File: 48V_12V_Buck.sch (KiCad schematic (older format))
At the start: 63 parts, among them Q4 CSD18534Q5A, Q5 CSD18540Q5B

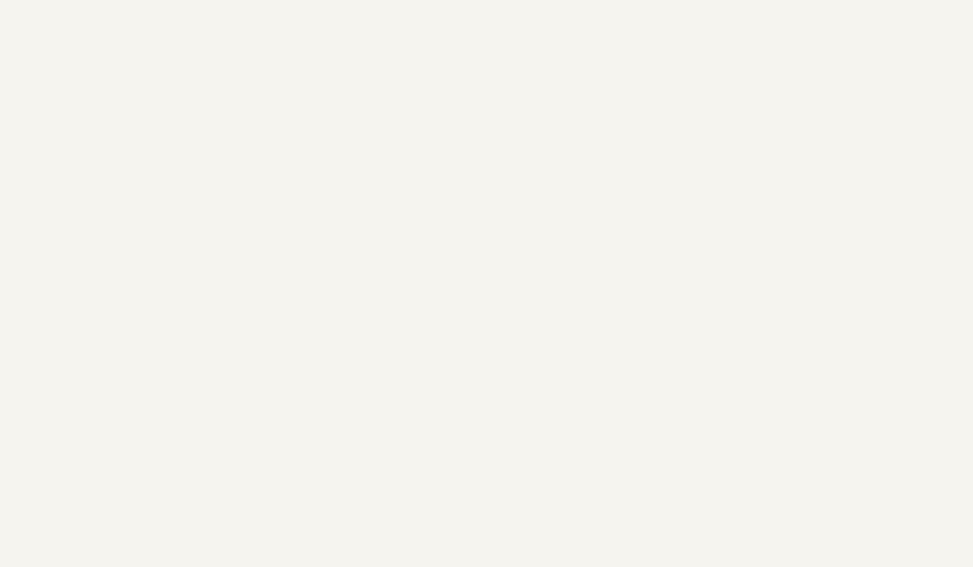
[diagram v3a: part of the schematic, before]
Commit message: Changed Bank13 deoupling caps and set the bank voltage to 2.5V
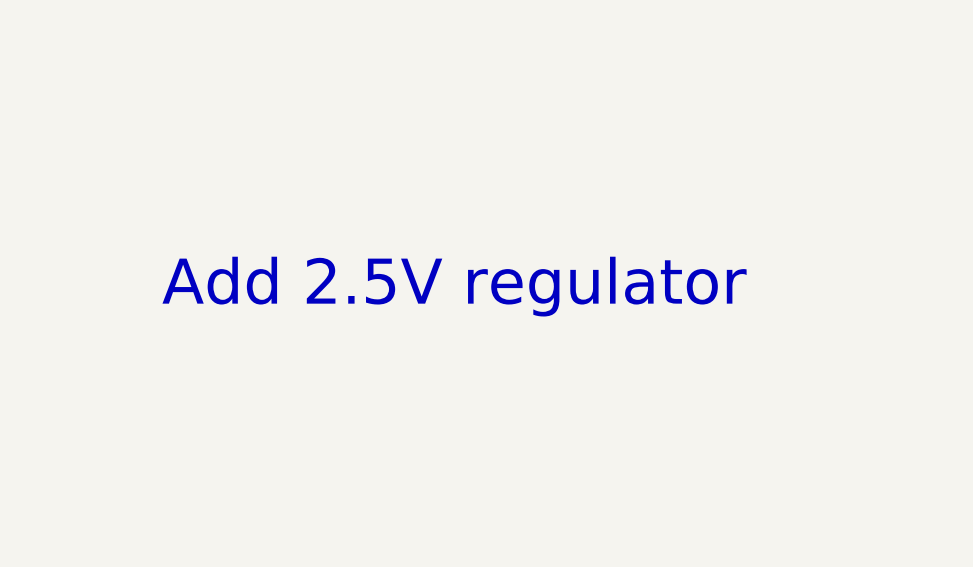
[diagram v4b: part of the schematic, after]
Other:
- note added: "Add 2.5V regulator"
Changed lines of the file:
@@
 Wire Wire Line
 	9500 8675 9550 8675
+Text Notes 12250 5900 0    197  ~ 0
+Add 2.5V regulator
 $EndSCHEMATC

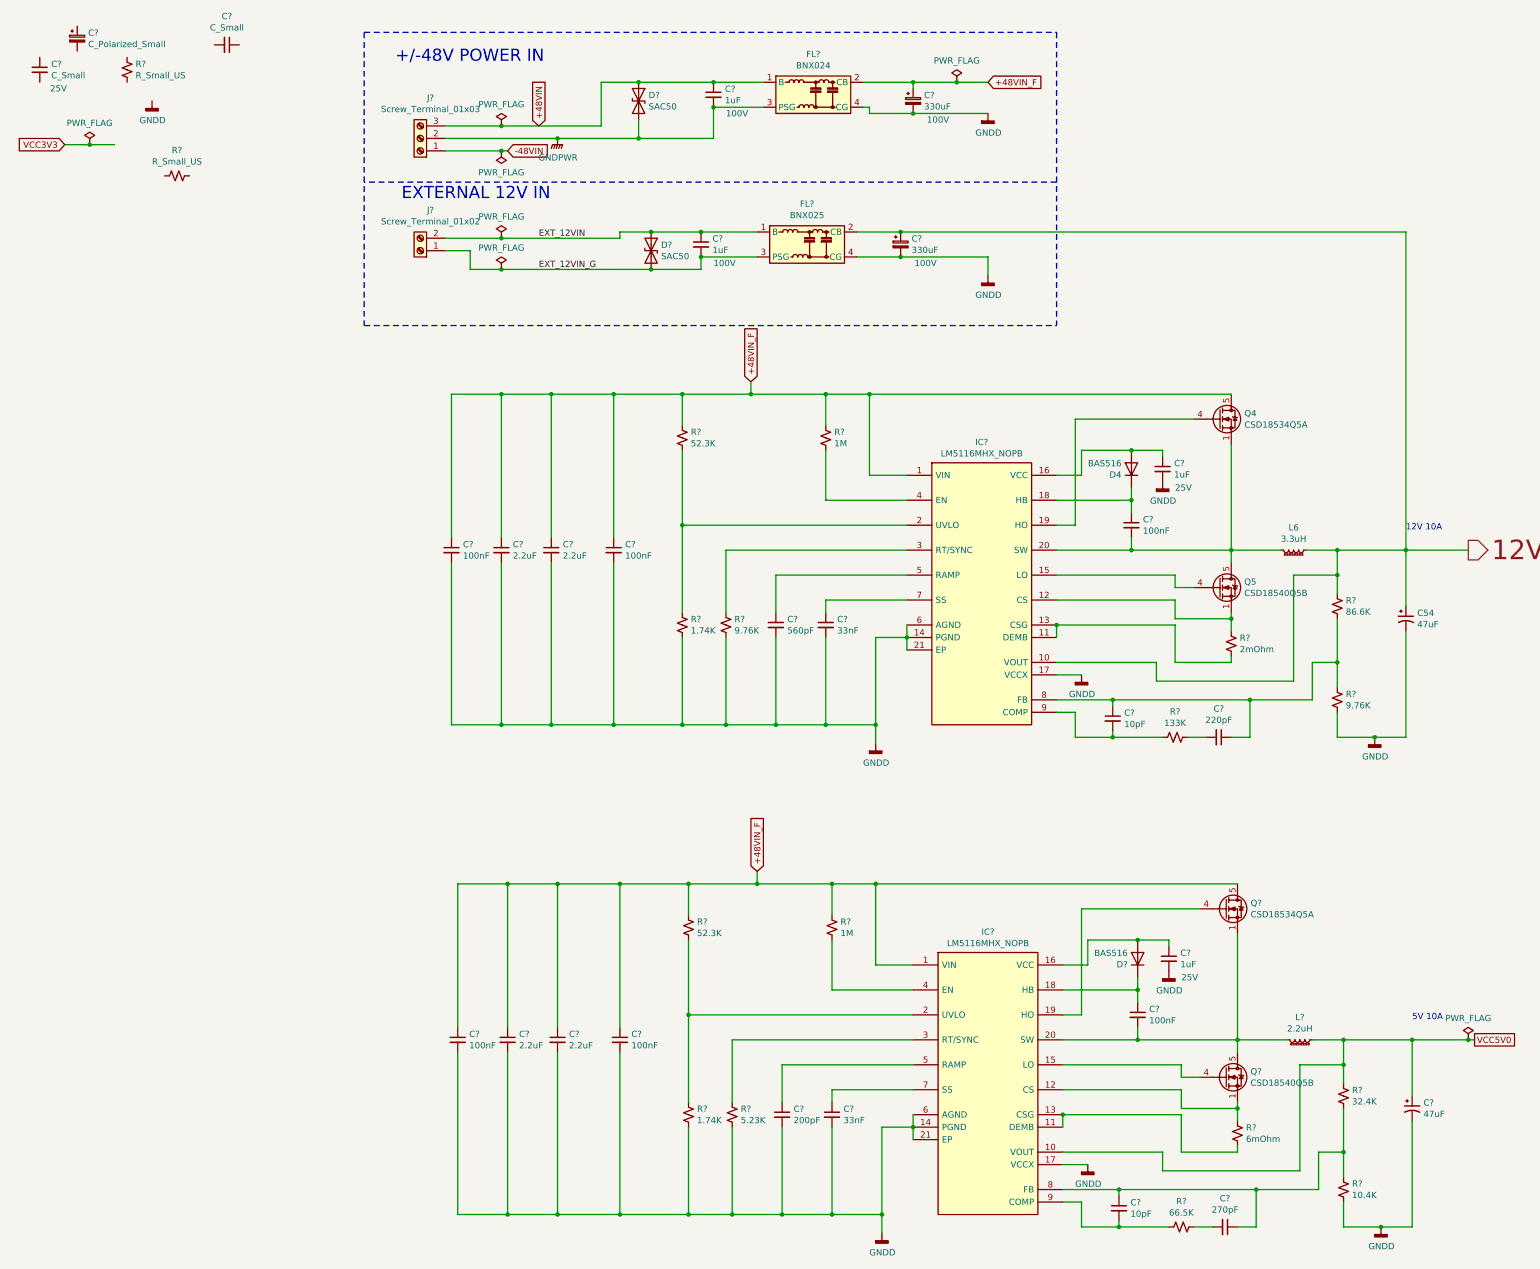
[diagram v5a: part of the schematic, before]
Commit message: PCB created and schematics annotated High speed connections added to the BTB
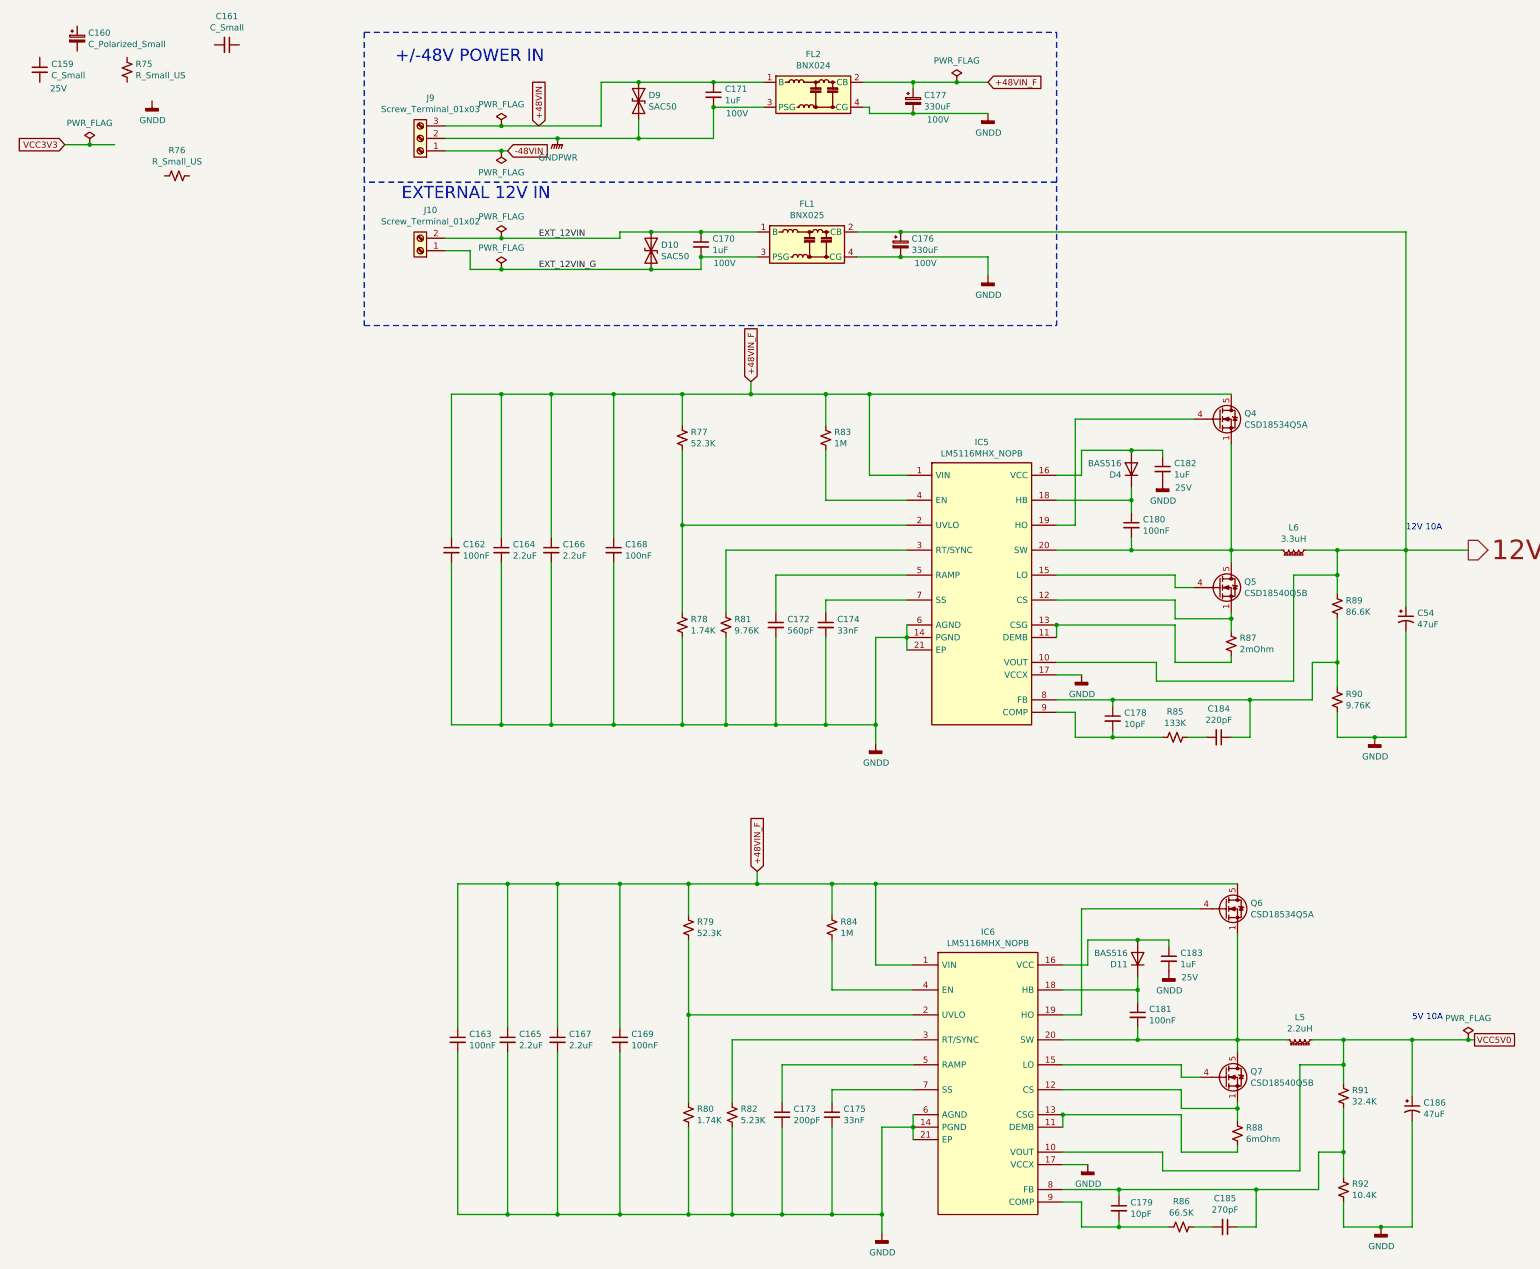
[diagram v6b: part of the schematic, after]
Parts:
- gave numbers to parts that had none: 58

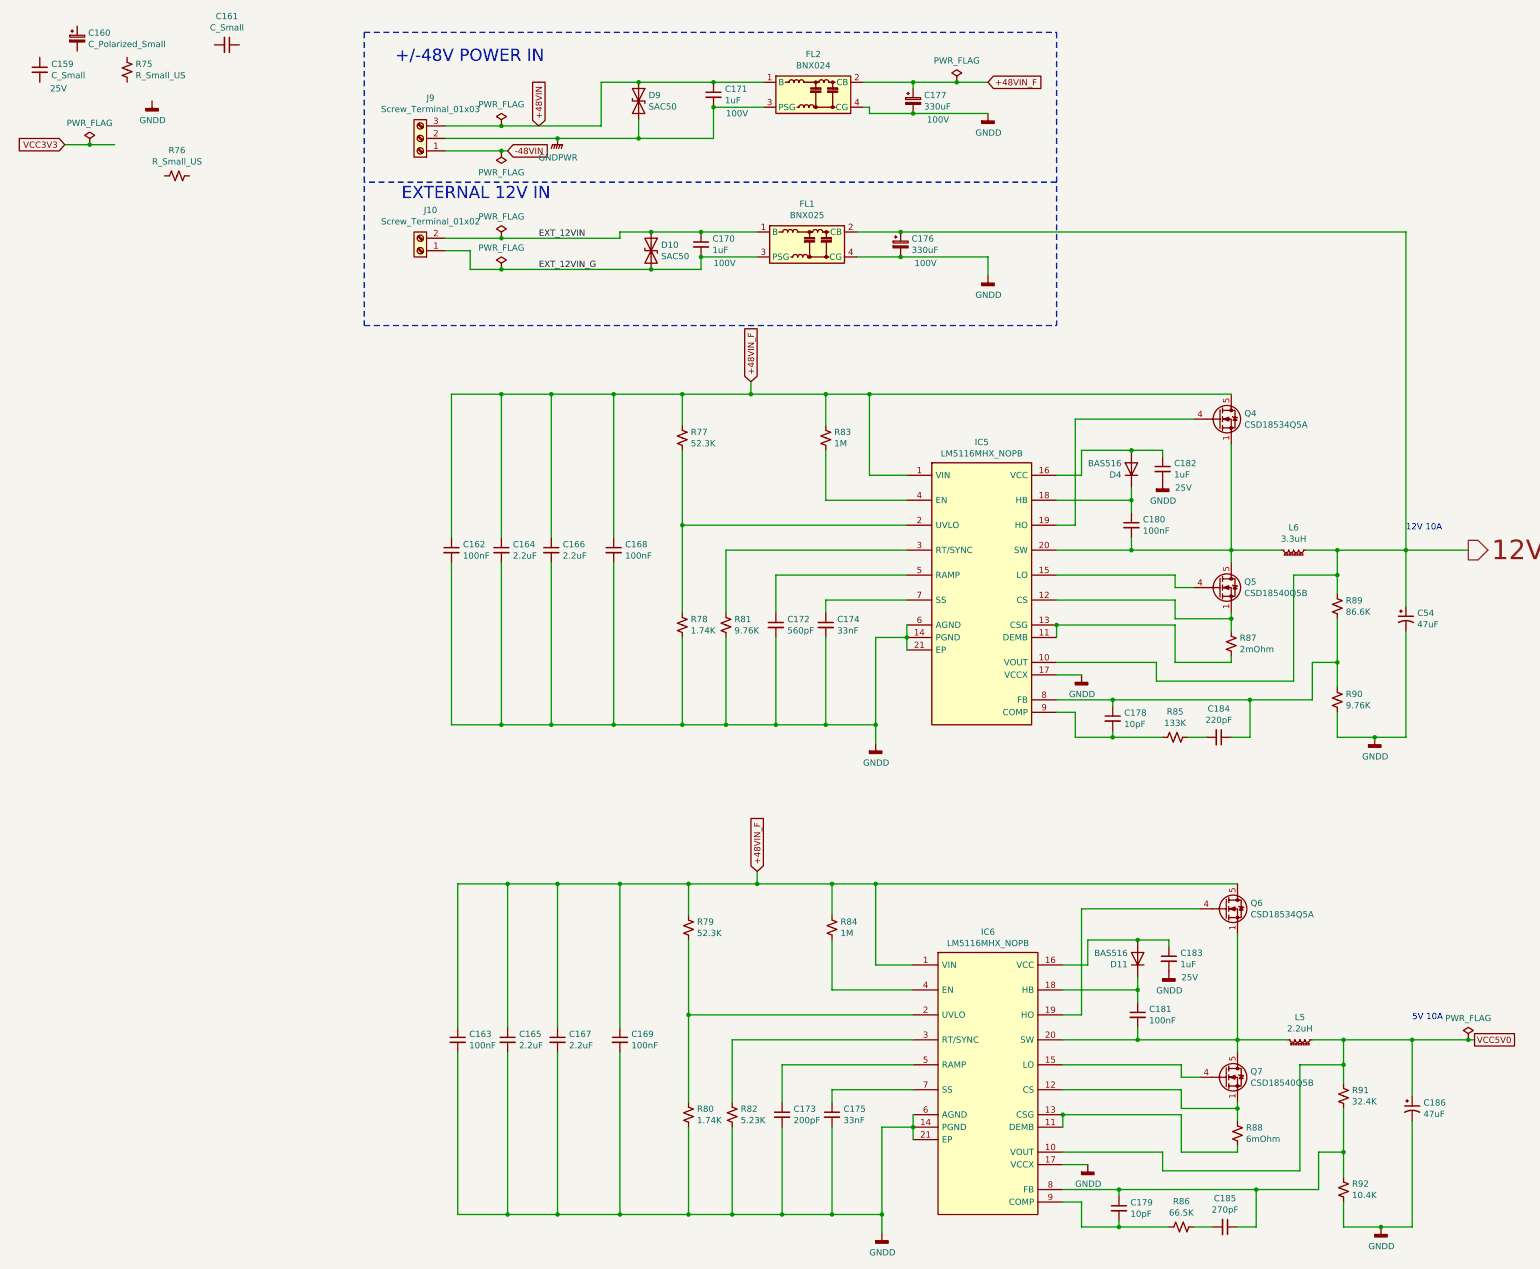
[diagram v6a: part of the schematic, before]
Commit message: Corrected PCB import errors
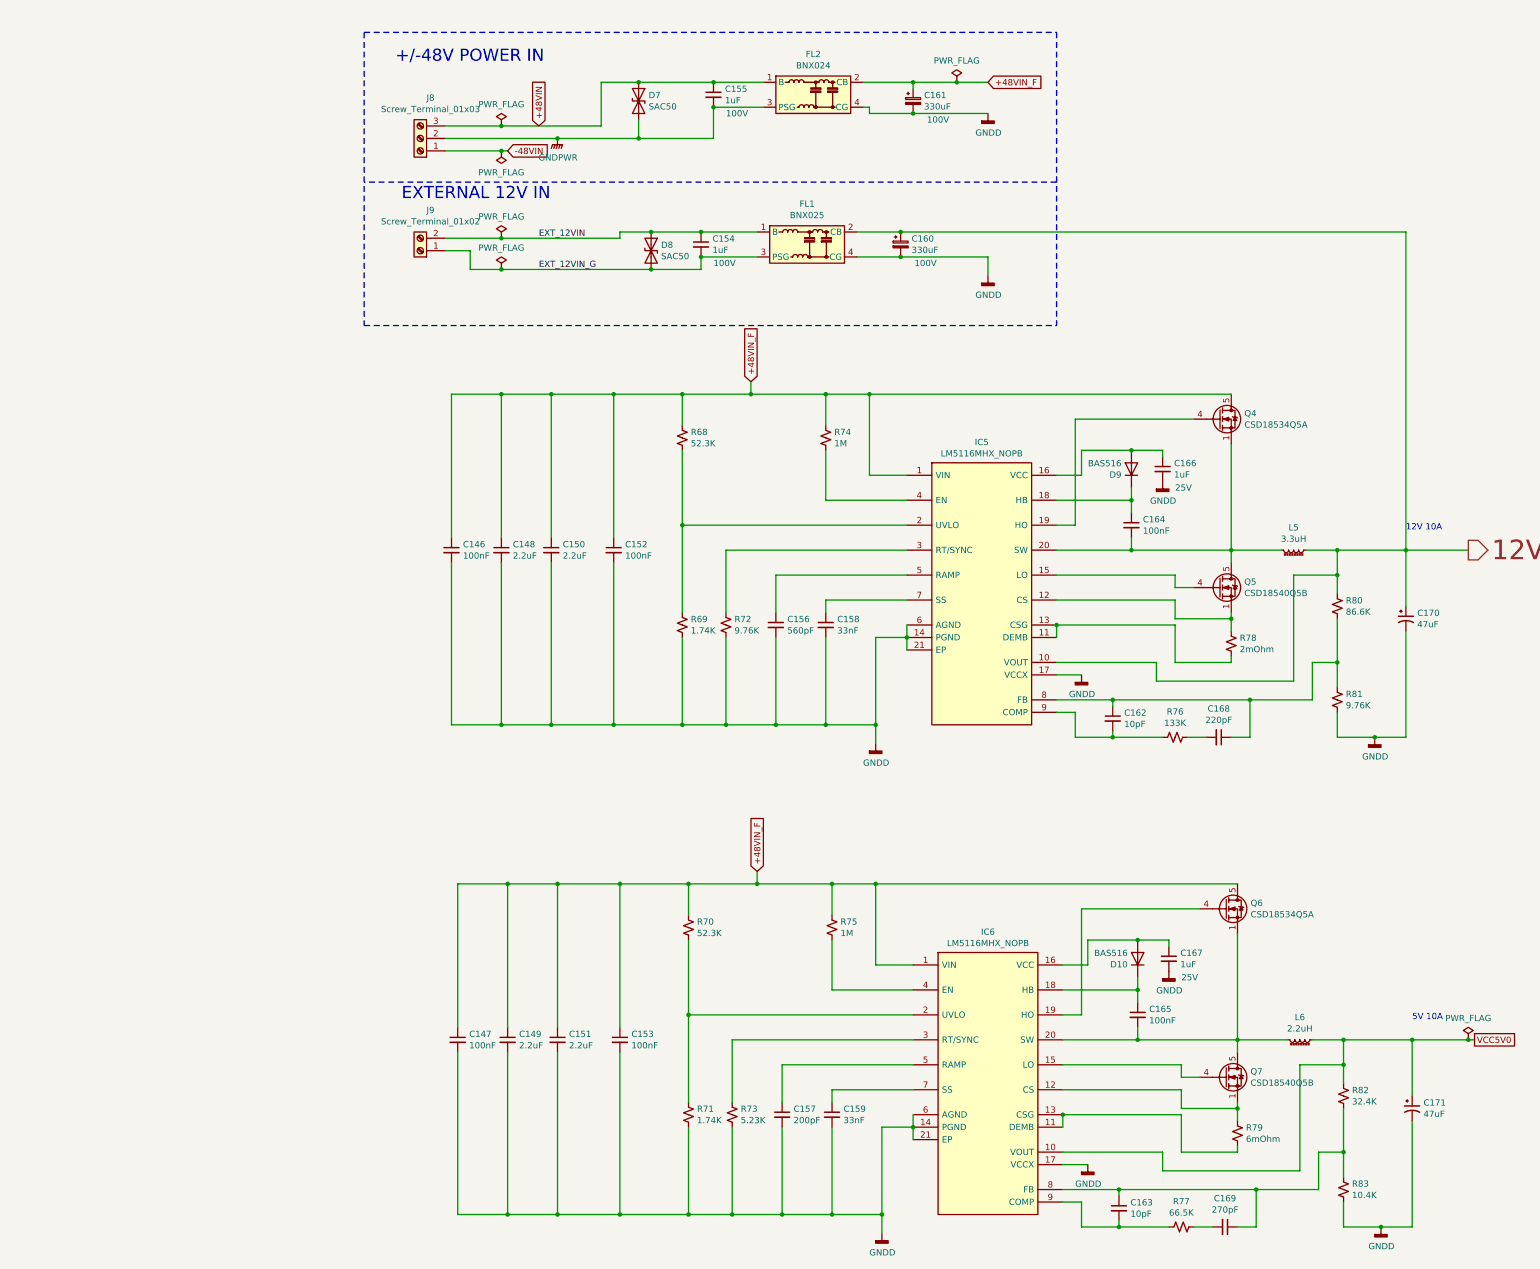
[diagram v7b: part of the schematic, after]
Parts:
- removed C159: C_Small, Capacitor_SMD:C_0603_1608Metric_Pad1.08x0.95mm_HandSolder, symbol Device:C_Small
- removed C160: C_Polarized_Small, Capacitor_Tantalum_SMD:CP_EIA-1608-10_AVX-L_Pad1.25x1.05mm_HandSolder, symbol Device:C_Polarized_Small
- removed C161: C_Small, symbol Device:C_Small
- removed R75, R76: R_Small_US, Resistor_SMD:R_0603_1608Metric_Pad0.98x0.95mm_HandSolder, symbol Device:R_Small_US
- renumbered C162 to C146, C163 to C147, C164 to C148, C165 to C149, C166 to C150, C167 to C151, C168 to C152, C169 to C153, C170 to C154, C171 to C155, C172 to C156, C173 to C157, C174 to C158, C175 to C159, C176 to C160, C177 to C161, C178 to C162, C179 to C163, C180 to C164, C181 to C165, C182 to C166, C183 to C167, C184 to C168, C185 to C169, C54 to C170, C186 to C171, D11 to D10, D9 to D7, D10 to D8, D4 to D9, J9 to J8, J10 to J9, L6 to L5, L5 to L6, R77 to R68, R78 to R69, R79 to R70, R80 to R71, R81 to R72, R82 to R73, R83 to R74, R84 to R75, R85 to R76, R86 to R77, R87 to R78, R88 to R79, R89 to R80, R90 to R81, R91 to R82, R92 to R83
